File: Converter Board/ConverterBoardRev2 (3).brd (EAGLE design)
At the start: 101.6 x 101.6 mm, 28 parts

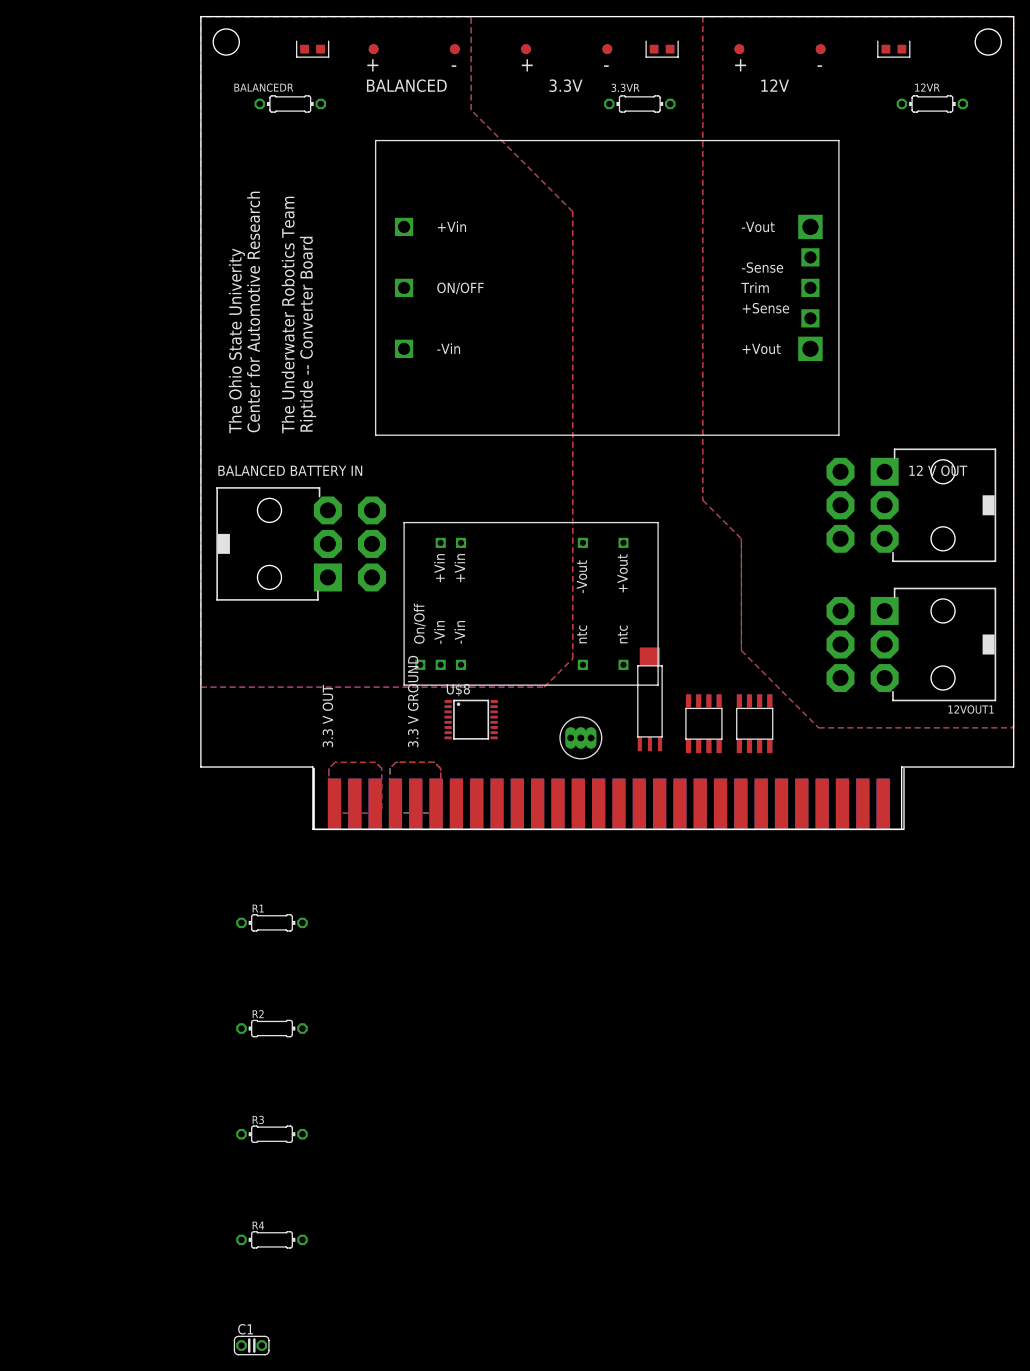
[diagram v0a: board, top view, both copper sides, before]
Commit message: Computer might blow up
Schematic done
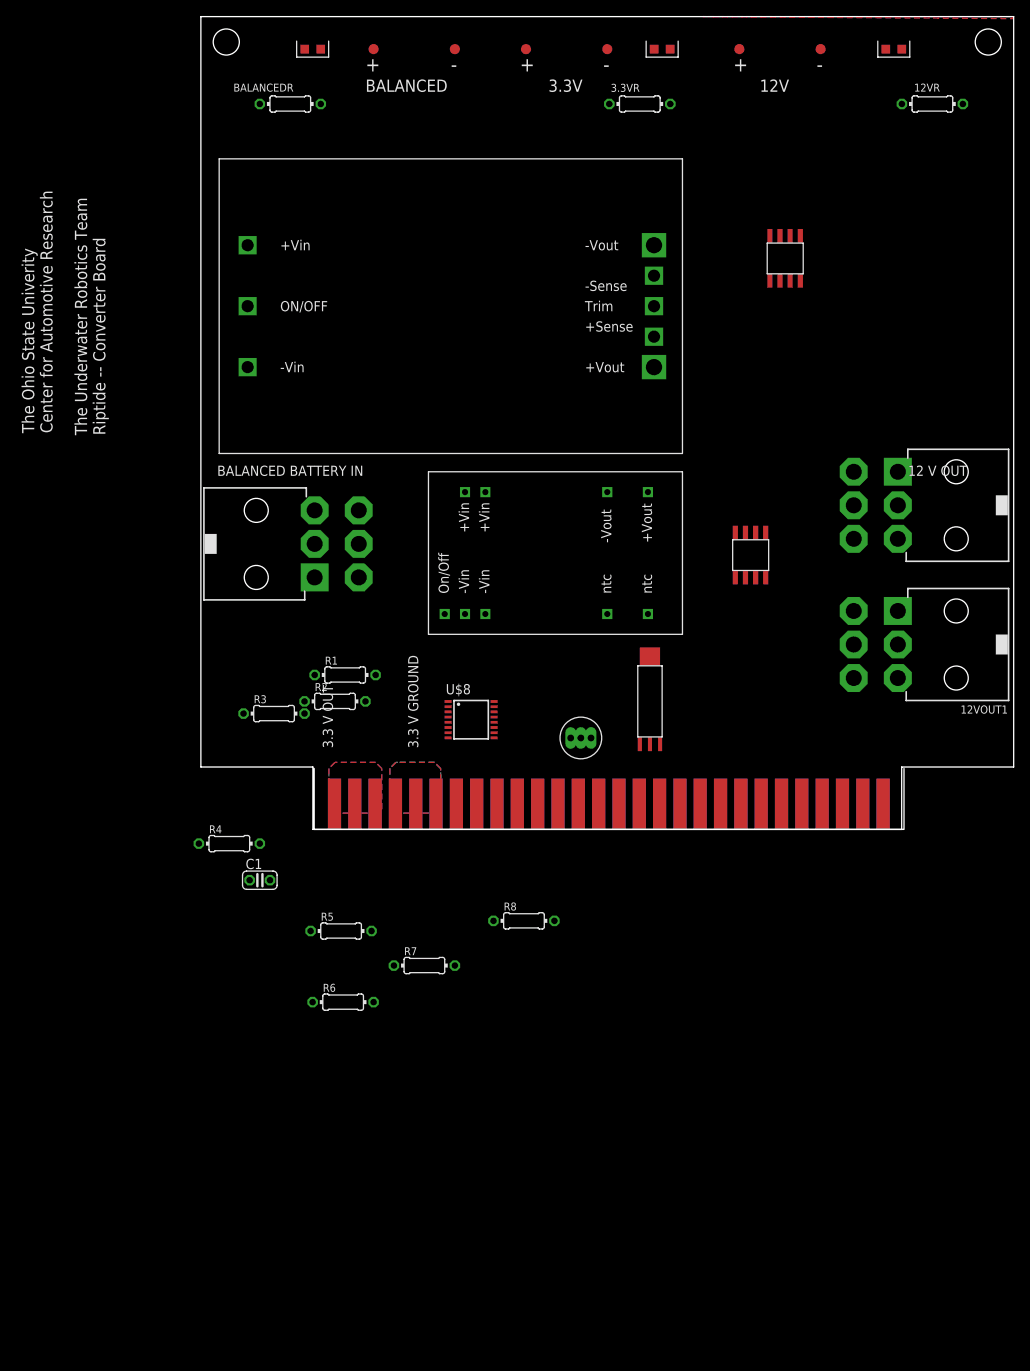
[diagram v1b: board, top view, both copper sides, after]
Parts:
- added R5, R6, R7, R8: (no value), resistor:0204/7
- moved U$4 58.3 mm to (71.1, 68.6)
- moved C1 58.2 mm to (7.37, -6.35)
- moved R3 52.6 mm to (9.14, 14.5)
- moved R4 49.8 mm to (3.56, -1.78)
- moved R2 41.6 mm to (16.8, 16.0)
- moved R1 32.3 mm to (18.0, 19.3)
- moved U$5 21.9 mm to (66.8, 31.5)
- moved U$1 19.7 mm to (2.29, 47.0)
- moved U$2 7.04 mm to (60.2, 24.4)
- moved BALANCEDRAWIN 1.65 mm to (14.2, 35.7)
- moved 12VOUT 1.65 mm to (87.1, 40.5)
- moved 12VOUT1 1.65 mm to (87.1, 23.1)
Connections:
- net N$2 renamed 3.3IDATA
- net N$3 renamed 12IDATA
- net N$5 renamed A0
- net N$6 renamed A1
- net N$7 renamed SCL
- net N$8 renamed SDA
- new net 12VDATA: R7.2, R8.1, U$8.IN2
- new net 3.3VDATA: R5.1, R6.1, U$8.IN3
- net 12V+: now also R7.1
- net 12V-: now also R8.2
- net 3.3V+: now also R5.2, R6.2
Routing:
- removed copper zone on layer 16, net 12V-
- removed copper zone on layer 1, net BALANCED+
- removed copper zone on layer 16, net BALANCED-
